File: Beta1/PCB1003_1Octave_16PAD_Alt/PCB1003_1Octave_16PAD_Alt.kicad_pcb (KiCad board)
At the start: 2 copper layers, 188.9 x 64 mm, 101 parts, among them P0 CONN_01X01, P1 CONN_01X01, P10 CONN_01X01, P100 CONN_01X01, P101 CONN_01X01, P102 CONN_01X01, P103 CONN_01X01, P104 CONN_01X01, P105 CONN_01X01, P106 CONN_01X01, P107 CONN_01X01, P108 CONN_01X01, P109 CONN_01X01, P11 CONN_01X01, P110 CONN_01X01, P111 CONN_01X01, P2 CONN_01X01, P200 CONN_01X01, P201 CONN_01X01, P202 CONN_01X01, P203 CONN_01X01, P204 CONN_01X01, P205 CONN_01X01, P206 CONN_01X01, P207 CONN_01X01, P208 CONN_01X01, P209 CONN_01X01, P210 CONN_01X01, P211 CONN_01X01, P3 CONN_01X01, P4 CONN_01X01, P5 CONN_01X01, P6 CONN_01X01, P7 CONN_01X01, P8 CONN_01X01, P9 CONN_01X01, U1 CPT112S, U100 CPT112S, U200 CPT112S

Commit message: Finished routing. Ready for proto.
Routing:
- net GND: track 0.00 -> 10592.5 mm, vias 0 -> 10
- net Net-(P211-Pad1): track 0.00 -> 178.6 mm, vias 0 -> 1
- net /PAD7: track 0.00 -> 170.2 mm, vias 0 -> 1
- net Net-(P107-Pad1): track 0.00 -> 163.6 mm, vias 0 -> 1
- net Net-(P210-Pad1): track 0.00 -> 150.4 mm, vias 0 -> 1
- net /PAD6: track 0.00 -> 150.0 mm, vias 0 -> 1
- net Net-(P209-Pad1): track 0.00 -> 144.5 mm, vias 0 -> 1
- net Net-(P106-Pad1): track 0.00 -> 142.2 mm, vias 0 -> 1
- net /PAD5: track 0.00 -> 130.6 mm, vias 0 -> 1
- net Net-(P208-Pad1): track 0.00 -> 127.7 mm, vias 0 -> 1
- net Net-(P207-Pad1): track 0.00 -> 127.5 mm, vias 0 -> 1
- net Net-(P105-Pad1): track 0.00 -> 120.8 mm, vias 0 -> 1
- net /PAD4: track 0.00 -> 109.0 mm, vias 0 -> 1
- net Net-(P206-Pad1): track 0.00 -> 104.5 mm, vias 0 -> 1
- net /SCL: track 0.00 -> 101.1 mm, vias 0 -> 2
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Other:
- board text added: "PCB1003_1OCTAVE_16PAD_Alt_2017-02-02 Beta-1 Believotron Wanderlust 1/2 H Keypad 1 Octave Piano, 16 Pads 6CH Analog Mezzanine Expansion headers"
- board text removed: "PCB1002_1OCTAVE_16PAD_2017-01-26 Beta-1 Believotron Wanderlust 1/2 H Keypad 1 Octave Piano, 16 Pads 6CH Analog Mezzanine Expansion headers"

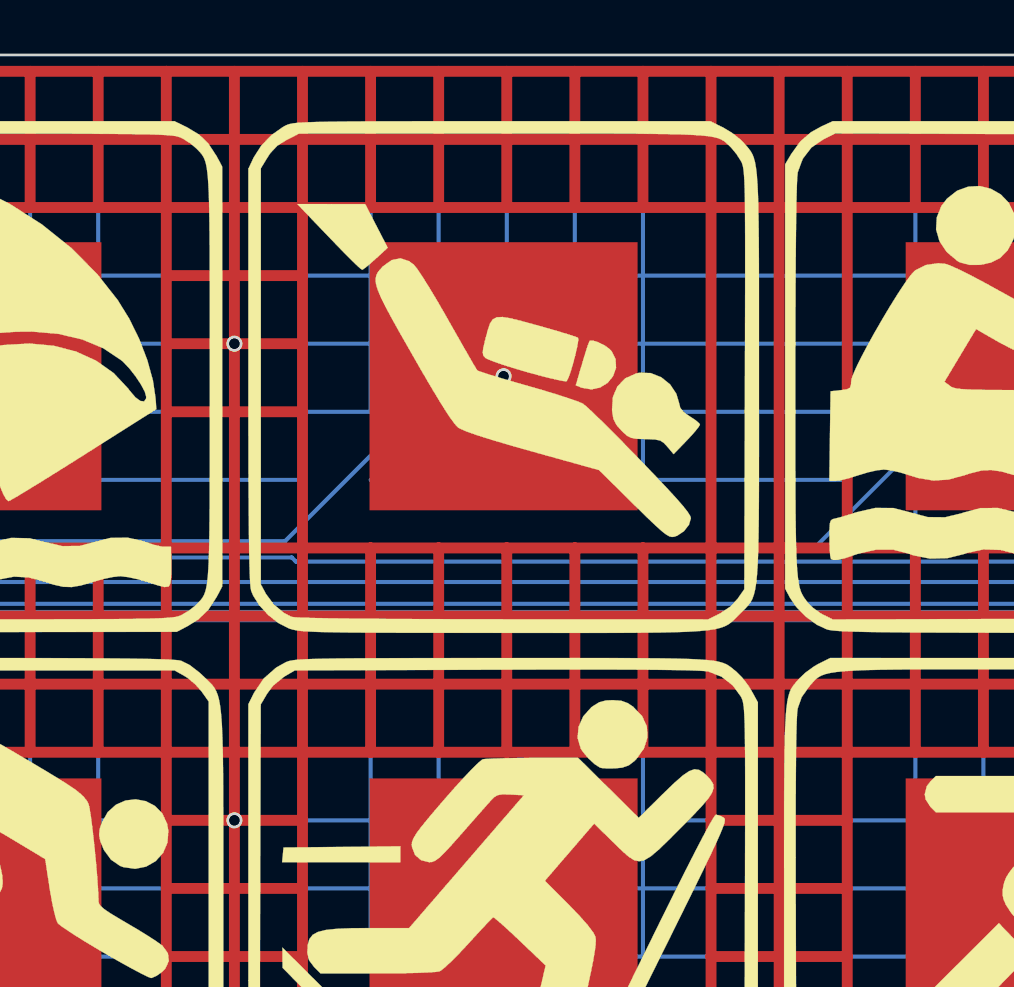
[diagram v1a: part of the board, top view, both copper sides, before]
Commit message: Filled in empty gnd hatch.
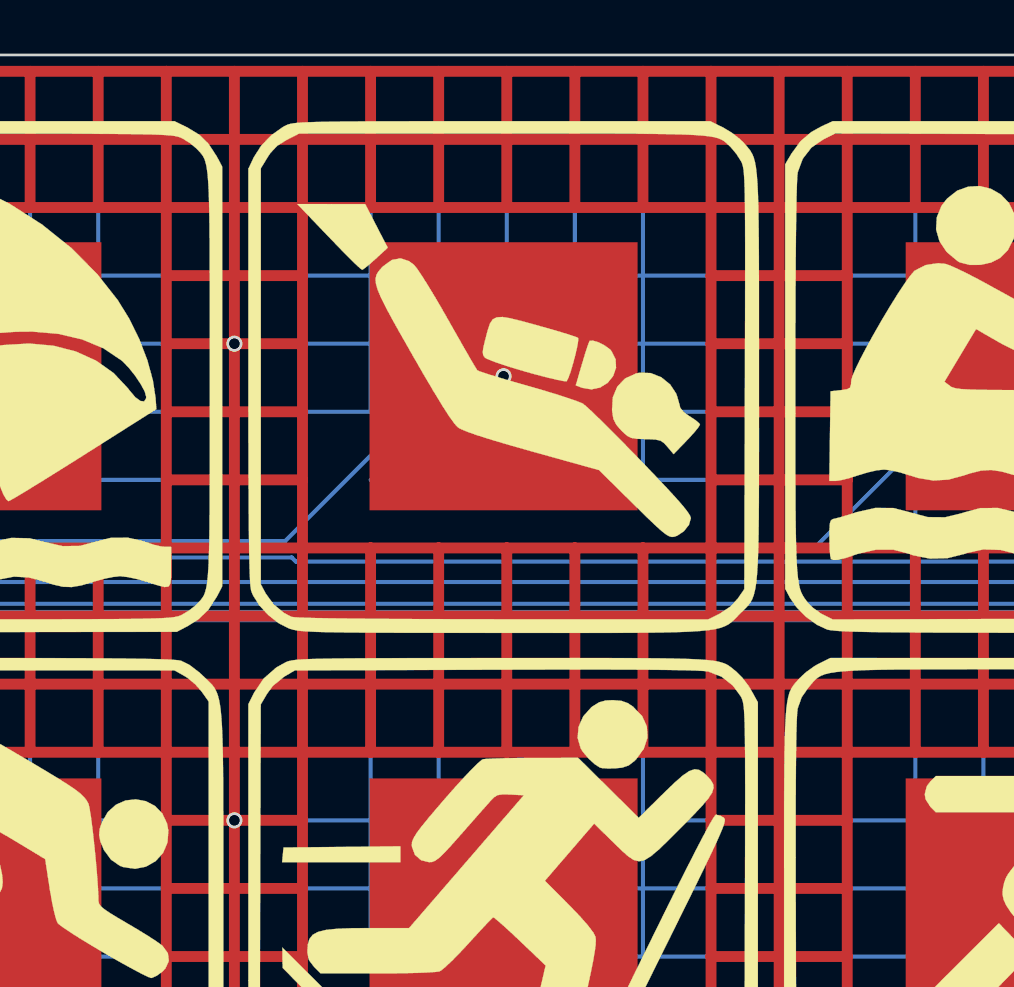
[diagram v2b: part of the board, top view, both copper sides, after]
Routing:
- net (no net): track 0.00 -> 1270.0 mm
- net GND: track 10592.5 -> 9347.9 mm

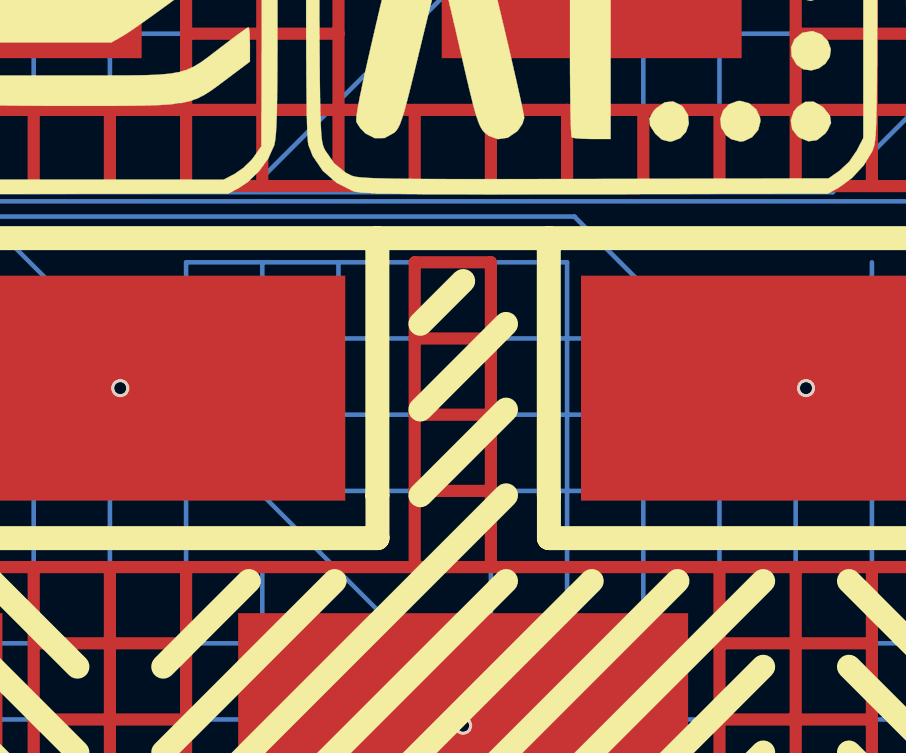
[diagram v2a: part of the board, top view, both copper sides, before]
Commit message: Filled in more gnd hatch.
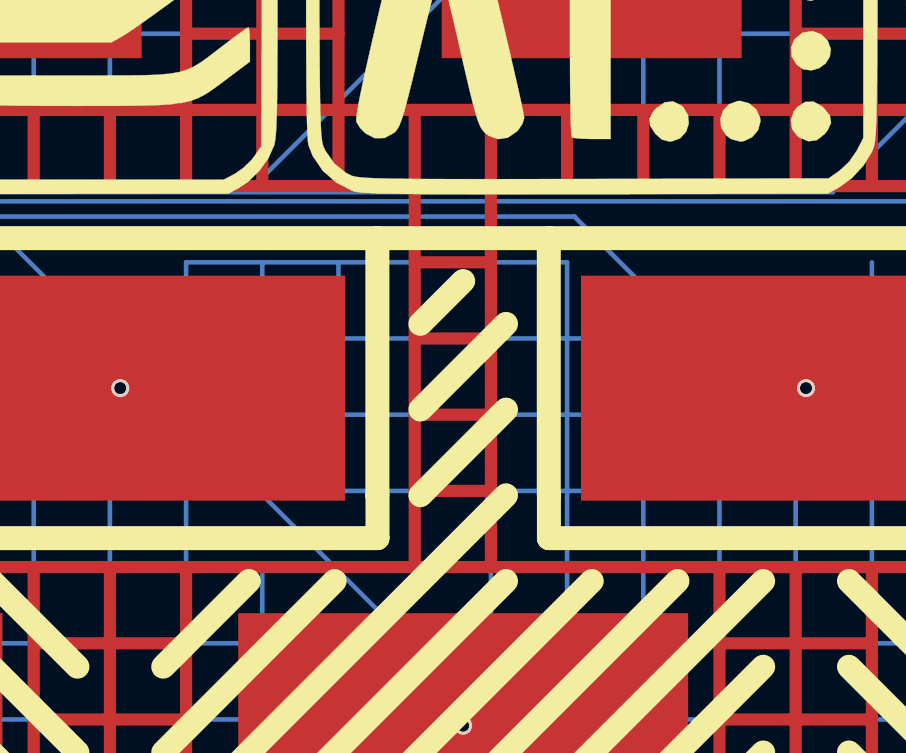
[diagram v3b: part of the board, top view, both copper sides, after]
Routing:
- net GND: track 9347.9 -> 9383.5 mm
- net (no net): track 1270.0 -> 1239.5 mm
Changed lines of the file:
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@@
     (thickness 1.6)
     (drawings 36)
-    (tracks 2066)
+    (tracks 2069)
     (zones 0)
     (modules 101)
@@
   (segment (start 187.96 -33.02) (end 182.88 -33.02) (width 0.4064) (layer F.Cu) (net 0))
   (segment (start 175.26 -10.16) (end 175.26 -22.86) (width 0.4064) (layer F.Cu) (net 0))
-  (segment (start 149.86 -12.7) (end 149.86 -15.24) (width 0.4064) (layer F.Cu) (net 0))
-  (segment (start 149.86 -10.16) (end 149.86 -12.7) (width 0.4064) (layer F.Cu) (net 0))
-  (segment (start 149.86 -12.7) (end 152.4 -12.7) (width 0.4064) (layer F.Cu) (net 0))
-  (segment (start 149.86 -15.24) (end 149.86 -17.78) (width 0.4064) (layer F.Cu) (net 0))
-  (segment (start 149.86 -15.24) (end 152.4 -15.24) (width 0.4064) (layer F.Cu) (net 0))
-  (segment (start 149.86 -17.78) (end 149.86 -20.32) (width 0.4064) (layer F.Cu) (net 0))
-  (segment (start 149.86 -17.78) (end 152.4 -17.78) (width 0.4064) (layer F.Cu) (net 0))
-  (segment (start 152.4 -20.32) (end 152.4 -10.16) (width 0.4064) (layer F.Cu) (net 0))
-  (segment (start 149.86 -20.32) (end 152.4 -20.32) (width 0.4064) (layer F.Cu) (net 0))
   (segment (start 127 -12.7) (end 129.54 -12.7) (width 0.4064) (layer F.Cu) (net 0))
   (segment (start 127 -15.24) (end 129.54 -15.24) (width 0.4064) (layer F.Cu) (net 0))
@@
   (segment (start 25.4 -15.24) (end 38.1 -15.24) (width 0.4064) (layer F.Cu) (net 0))
   (segment (start 27.94 -60.96) (end 185.42 -60.96) (width 0.4064) (layer F.Cu) (net 0))
+  (segment (start 149.86 -12.7) (end 149.86 -15.24) (width 0.4064) (layer F.Cu) (net 1))
+  (segment (start 149.86 -10.16) (end 149.86 -12.7) (width 0.4064) (layer F.Cu) (net 1))
+  (segment (start 149.86 -12.7) (end 152.4 -12.7) (width 0.4064) (layer F.Cu) (net 1))
+  (segment (start 149.86 -15.24) (end 149.86 -17.78) (width 0.4064) (layer F.Cu) (net 1))
+  (segment (start 152.4 -10.16) (end 152.4 -15.24) (width 0.4064) (layer F.Cu) (net 1))
+  (segment (start 152.4 -15.24) (end 152.4 -17.78) (width 0.4064) (layer F.Cu) (net 1))
+  (segment (start 149.86 -15.24) (end 152.4 -15.24) (width 0.4064) (layer F.Cu) (net 1))
+  (segment (start 149.86 -17.78) (end 149.86 -22.86) (width 0.4064) (layer F.Cu) (net 1))
+  (segment (start 152.4 -17.78) (end 152.4 -22.86) (width 0.4064) (layer F.Cu) (net 1))
+  (segment (start 149.86 -17.78) (end 152.4 -17.78) (width 0.4064) (layer F.Cu) (net 1))
+  (segment (start 149.86 -20.32) (end 152.4 -20.32) (width 0.4064) (layer F.Cu) (net 1))
+  (segment (start 152.4 -10.16) (end 160.02 -10.16) (width 0.4064) (layer F.Cu) (net 1))
+  (segment (start 142.24 -10.16) (end 152.4 -10.16) (width 0.4064) (layer F.Cu) (net 1))
   (segment (start 63.5 -53.34) (end 63.5 -55.88) (width 0.4064) (layer F.Cu) (net 1))
   (segment (start 63.5 -50.8) (end 63.5 -53.34) (width 0.4064) (layer F.Cu) (net 1))
@@
   (segment (start 160.02 -10.16) (end 162.56 -10.16) (width 0.4064) (layer F.Cu) (net 1))
   (segment (start 162.56 -10.16) (end 162.56 -2.54) (width 0.4064) (layer F.Cu) (net 1))
-  (segment (start 142.24 -10.16) (end 160.02 -10.16) (width 0.4064) (layer F.Cu) (net 1))
   (segment (start 137.16 -5.08) (end 137.16 -2.54) (width 0.4064) (layer F.Cu) (net 1))
   (segment (start 137.16 -7.62) (end 137.16 -5.08) (width 0.4064) (layer F.Cu) (net 1))

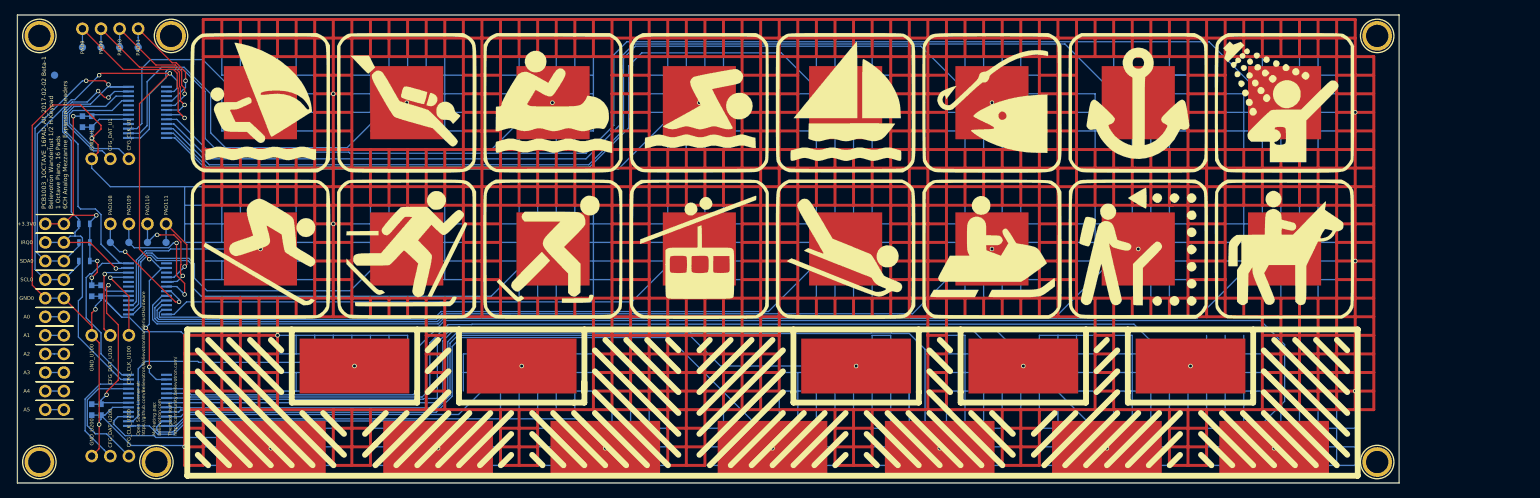
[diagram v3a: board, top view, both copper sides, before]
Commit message: Pin swap reroute WIP.
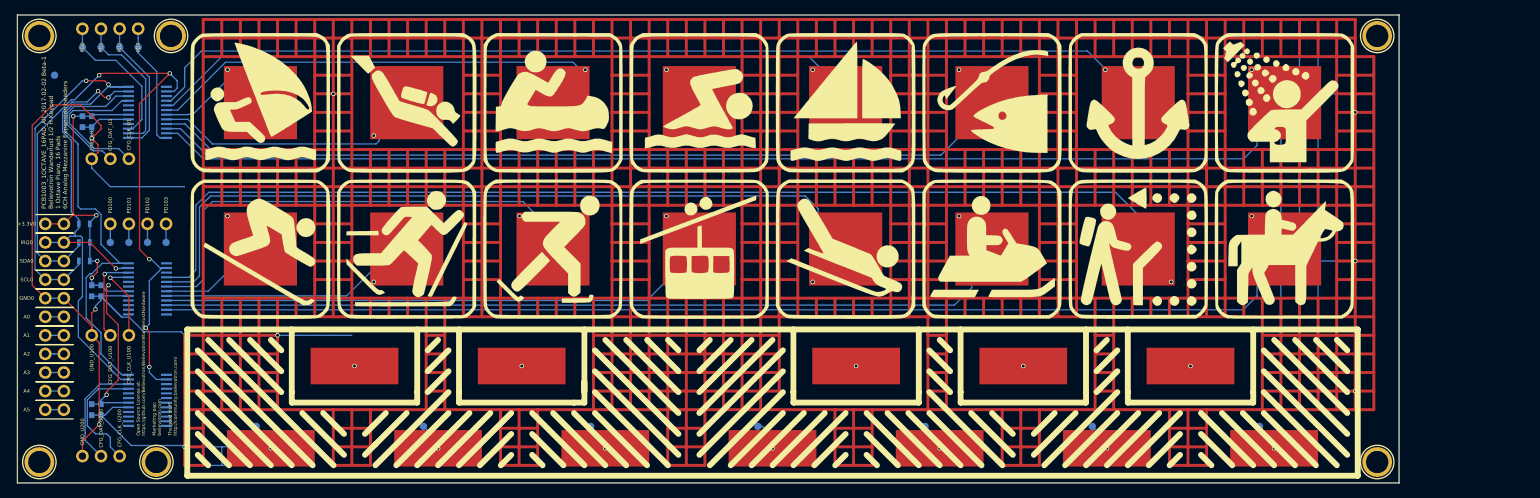
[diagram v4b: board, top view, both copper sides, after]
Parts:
- UKEY0: footprint Liberry:Keyboard_1_Octave_20CM -> Liberry:Keyboard_1_Octave_20CM_V2
- moved TP111 6.67 mm to (159.0, -28.0)
- moved TP9 6.52 mm to (79.0, -56.0)
- moved TP10 4.26 mm to (112.0, -56.0)
- moved TP8 4.26 mm to (32.0, -56.0)
- moved TP11 4.26 mm to (152.0, -56.0)
- moved TP4 4.26 mm to (172.0, -56.0)
- moved TP5 4.26 mm to (132.0, -56.0)
- moved TP104 4.07 mm to (172.0, -36.0)
- moved TP106 3.95 mm to (93.0, -36.0)
- moved TP109 3.95 mm to (73.0, -36.0)
- moved TP6 3.95 mm to (93.0, -56.0)
- moved TP108 3.95 mm to (33.0, -36.0)
- moved TP105 3.95 mm to (133.0, -36.0)
- moved TP110 3.59 mm to (112.0, -29.0)
- moved TP107 3.59 mm to (52.0, -29.0)
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- renumbered PAD8 to PD0, PAD9 to PD1, PAD108 to PD100, PAD109 to PD101, PAD110 to PD102, PAD111 to PD103, PAD10 to PD2, PAD11 to PD3, P8 to TP0, P9 to TP1, P4 to TP10, P108 to TP100, P109 to TP101, P110 to TP102, P111 to TP103, P107 to TP104, P105 to TP105, P103 to TP106, P101 to TP107, P100 to TP108, P102 to TP109, P6 to TP11, P104 to TP110, P106 to TP111, P10 to TP2, P205 to TP200, P202 to TP201, P200 to TP202, P204 to TP203, P207 to TP204, P209 to TP205, P211 to TP206, P201 to TP207, P203 to TP208, P206 to TP209, P208 to TP210, P210 to TP211, P11 to TP3, P7 to TP4, P5 to TP5, P3 to TP6, P1 to TP7, P0 to TP8, P2 to TP9
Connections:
- net /PAD5 renamed /CHIP_05
- net Net-(P105-Pad1) renamed /CHIP_105
- PAD0 pad 1: /PAD0 -> /CHIP_08
- PAD1 pad 1: /PAD1 -> /CHIP_07
- PAD100 pad 1: Net-(P100-Pad1) -> /CHIP_108
- PAD101 pad 1: Net-(P101-Pad1) -> /CHIP_107
- PAD102 pad 1: Net-(P102-Pad1) -> /CHIP_109
- PAD103 pad 1: Net-(P103-Pad1) -> /CHIP_106
- PAD104 pad 1: Net-(P104-Pad1) -> /CHIP_110
- PAD106 pad 1: Net-(P106-Pad1) -> /CHIP_111
- PAD107 pad 1: Net-(P107-Pad1) -> /CHIP_104
- PAD2 pad 1: /PAD2 -> /CHIP_09
- PAD3 pad 1: /PAD3 -> /CHIP_06
- PAD4 pad 1: /PAD4 -> /CHIP_10
- PAD6 pad 1: /PAD6 -> /CHIP_11
- PAD7 pad 1: /PAD7 -> /CHIP_04
- PD0 pad 1: Net-(P8-Pad1) -> Net-(PD0-Pad1)
- PD1 pad 1: Net-(P9-Pad1) -> Net-(PD1-Pad1)
- PD100 pad 1: Net-(P108-Pad1) -> Net-(PD100-Pad1)
- PD101 pad 1: Net-(P109-Pad1) -> Net-(PD101-Pad1)
- PD102 pad 1: Net-(P110-Pad1) -> Net-(PD102-Pad1)
- PD103 pad 1: Net-(P111-Pad1) -> Net-(PD103-Pad1)
- PD2 pad 1: Net-(P10-Pad1) -> Net-(PD2-Pad1)
- PD3 pad 1: Net-(P11-Pad1) -> Net-(PD3-Pad1)
- TP0 pad 1: Net-(P8-Pad1) -> Net-(PD0-Pad1)
- TP1 pad 1: Net-(P9-Pad1) -> Net-(PD1-Pad1)
- TP10 pad 1: /PAD4 -> /CHIP_10
- TP100 pad 1: Net-(P108-Pad1) -> Net-(PD100-Pad1)
- TP101 pad 1: Net-(P109-Pad1) -> Net-(PD101-Pad1)
- TP102 pad 1: Net-(P110-Pad1) -> Net-(PD102-Pad1)
- TP104 pad 1: Net-(P107-Pad1) -> /CHIP_104
- TP106 pad 1: Net-(P103-Pad1) -> /CHIP_106
- TP107 pad 1: Net-(P101-Pad1) -> /CHIP_107
- TP108 pad 1: Net-(P100-Pad1) -> /CHIP_108
- TP109 pad 1: Net-(P102-Pad1) -> /CHIP_109
- TP11 pad 1: /PAD6 -> /CHIP_11
- TP110 pad 1: Net-(P104-Pad1) -> /CHIP_110
- TP111 pad 1: Net-(P106-Pad1) -> /CHIP_111
- TP2 pad 1: Net-(P10-Pad1) -> Net-(PD2-Pad1)
- TP200 pad 1: Net-(P205-Pad1) -> /CHIP_200
- TP201 pad 1: Net-(P202-Pad1) -> /CHIP_201
- TP202 pad 1: Net-(P200-Pad1) -> /CHIP_202
- TP203 pad 1: Net-(P204-Pad1) -> /CHIP_203
- TP204 pad 1: Net-(P207-Pad1) -> /CHIP_204
- TP205 pad 1: Net-(P209-Pad1) -> /CHIP_205
- TP206 pad 1: Net-(P211-Pad1) -> /CHIP_206
- TP207 pad 1: Net-(P201-Pad1) -> /CHIP_207
- TP208 pad 1: Net-(P203-Pad1) -> /CHIP_208
- TP209 pad 1: Net-(P206-Pad1) -> /CHIP_209
- TP210 pad 1: Net-(P208-Pad1) -> /CHIP_210
- TP211 pad 1: Net-(P210-Pad1) -> /CHIP_211
- TP3 pad 1: Net-(P11-Pad1) -> Net-(PD3-Pad1)
- TP4 pad 1: /PAD7 -> /CHIP_04
- TP6 pad 1: /PAD3 -> /CHIP_06
- TP7 pad 1: /PAD1 -> /CHIP_07
- TP8 pad 1: /PAD0 -> /CHIP_08
- TP9 pad 1: /PAD2 -> /CHIP_09
- U1 pad 1: /PAD2 -> Net-(PD2-Pad1)
- U1 pad 16: Net-(P11-Pad1) -> /CHIP_11
- U1 pad 17: Net-(P10-Pad1) -> /CHIP_10
- U1 pad 18: Net-(P9-Pad1) -> /CHIP_09
- U1 pad 19: Net-(P8-Pad1) -> /CHIP_08
- U1 pad 2: /PAD1 -> Net-(PD1-Pad1)
- U1 pad 20: /PAD7 -> /CHIP_07
- U1 pad 21: /PAD6 -> /CHIP_06
- U1 pad 23: /PAD4 -> /CHIP_04
- U1 pad 24: /PAD3 -> Net-(PD3-Pad1)
- U1 pad 3: /PAD0 -> Net-(PD0-Pad1)
- U100 pad 1: Net-(P102-Pad1) -> Net-(PD102-Pad1)
- U100 pad 16: Net-(P111-Pad1) -> /CHIP_111
- U100 pad 17: Net-(P110-Pad1) -> /CHIP_110
- U100 pad 18: Net-(P109-Pad1) -> /CHIP_109
- U100 pad 19: Net-(P108-Pad1) -> /CHIP_108
- U100 pad 2: Net-(P101-Pad1) -> Net-(PD101-Pad1)
- U100 pad 20: Net-(P107-Pad1) -> /CHIP_107
- U100 pad 21: Net-(P106-Pad1) -> /CHIP_106
- U100 pad 23: Net-(P104-Pad1) -> /CHIP_104
- U100 pad 24: Net-(P103-Pad1) -> Net-(PD103-Pad1)
- U100 pad 3: Net-(P100-Pad1) -> Net-(PD100-Pad1)
- U200 pad 1: Net-(P202-Pad1) -> /CHIP_202
- U200 pad 16: Net-(P211-Pad1) -> /CHIP_211
- U200 pad 17: Net-(P210-Pad1) -> /CHIP_210
- U200 pad 18: Net-(P209-Pad1) -> /CHIP_209
- U200 pad 19: Net-(P208-Pad1) -> /CHIP_208
- U200 pad 2: Net-(P201-Pad1) -> /CHIP_201
- U200 pad 20: Net-(P207-Pad1) -> /CHIP_207
- U200 pad 21: Net-(P206-Pad1) -> /CHIP_206
- U200 pad 22: Net-(P205-Pad1) -> /CHIP_205
- U200 pad 23: Net-(P204-Pad1) -> /CHIP_204
- U200 pad 24: Net-(P203-Pad1) -> /CHIP_203
- U200 pad 3: Net-(P200-Pad1) -> /CHIP_200
- UKEY0 pad 1: Net-(P200-Pad1) -> /CHIP_200
- UKEY0 pad 10: Net-(P209-Pad1) -> /CHIP_209
- UKEY0 pad 11: Net-(P210-Pad1) -> /CHIP_210
- UKEY0 pad 12: Net-(P211-Pad1) -> /CHIP_211
- UKEY0 pad 2: Net-(P201-Pad1) -> /CHIP_201
- UKEY0 pad 3: Net-(P202-Pad1) -> /CHIP_202
- UKEY0 pad 4: Net-(P203-Pad1) -> /CHIP_203
- UKEY0 pad 5: Net-(P204-Pad1) -> /CHIP_204
- UKEY0 pad 6: Net-(P205-Pad1) -> /CHIP_205
- UKEY0 pad 7: Net-(P206-Pad1) -> /CHIP_206
- UKEY0 pad 8: Net-(P207-Pad1) -> /CHIP_207
- UKEY0 pad 9: Net-(P208-Pad1) -> /CHIP_208
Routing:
- net GND: track 9383.5 -> 3440.4 mm, vias 10 -> 5
- net (no net): track 1239.5 -> 1841.5 mm, vias 0 -> 4
- net Net-(P211-Pad1): track 178.6 -> 0.00 mm, vias 1 -> 0
- net /PAD7: track 170.2 -> 0.00 mm, vias 1 -> 0
- net Net-(P107-Pad1): track 163.6 -> 0.00 mm, vias 1 -> 0
- net /CHIP_04: track 0.00 -> 162.0 mm, vias 0 -> 1
- net /CHIP_104: track 0.00 -> 161.8 mm, vias 0 -> 1
- net /CHIP_111: track 0.00 -> 155.7 mm, vias 0 -> 1
- net Net-(P210-Pad1): track 150.4 -> 0.00 mm, vias 1 -> 0
- net /PAD6: track 150.0 -> 0.00 mm, vias 1 -> 0
- net Net-(P209-Pad1): track 144.5 -> 0.00 mm, vias 1 -> 0
- net Net-(P106-Pad1): track 142.2 -> 0.00 mm, vias 1 -> 0
- net /CHIP_11: track 0.00 -> 135.8 mm, vias 0 -> 1
- net Net-(P208-Pad1): track 127.7 -> 0.00 mm, vias 1 -> 0
- net Net-(P207-Pad1): track 127.5 -> 0.00 mm, vias 1 -> 0
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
